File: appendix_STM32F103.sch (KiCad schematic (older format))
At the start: 69 parts, among them J201 Micro_SD_Card_Det, J202 Conn_02x05_Odd_Even, J203 Conn_02x20_Odd_Even, J204 Conn_ARM_JTAG_SWD_10, SW201 SW_Push, SW202 SW_Push, SW203 SW_Push, U201 STM32F103ZETx, U202 NTS0104PW-Q100J, U203 NTS0104PW-Q100J, X201 SG-210STF

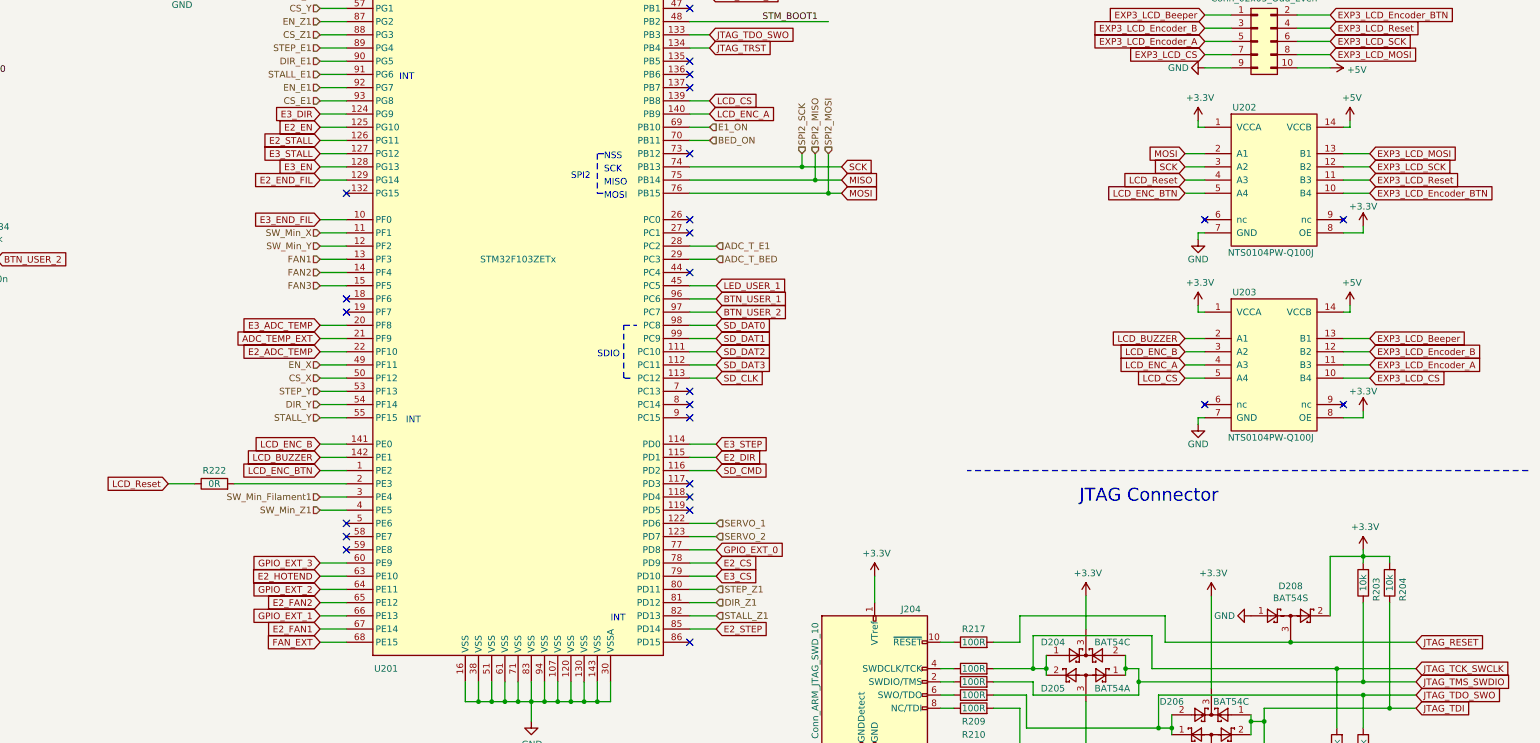
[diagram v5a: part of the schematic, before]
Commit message: changed Layout to use all Interrupt Pins
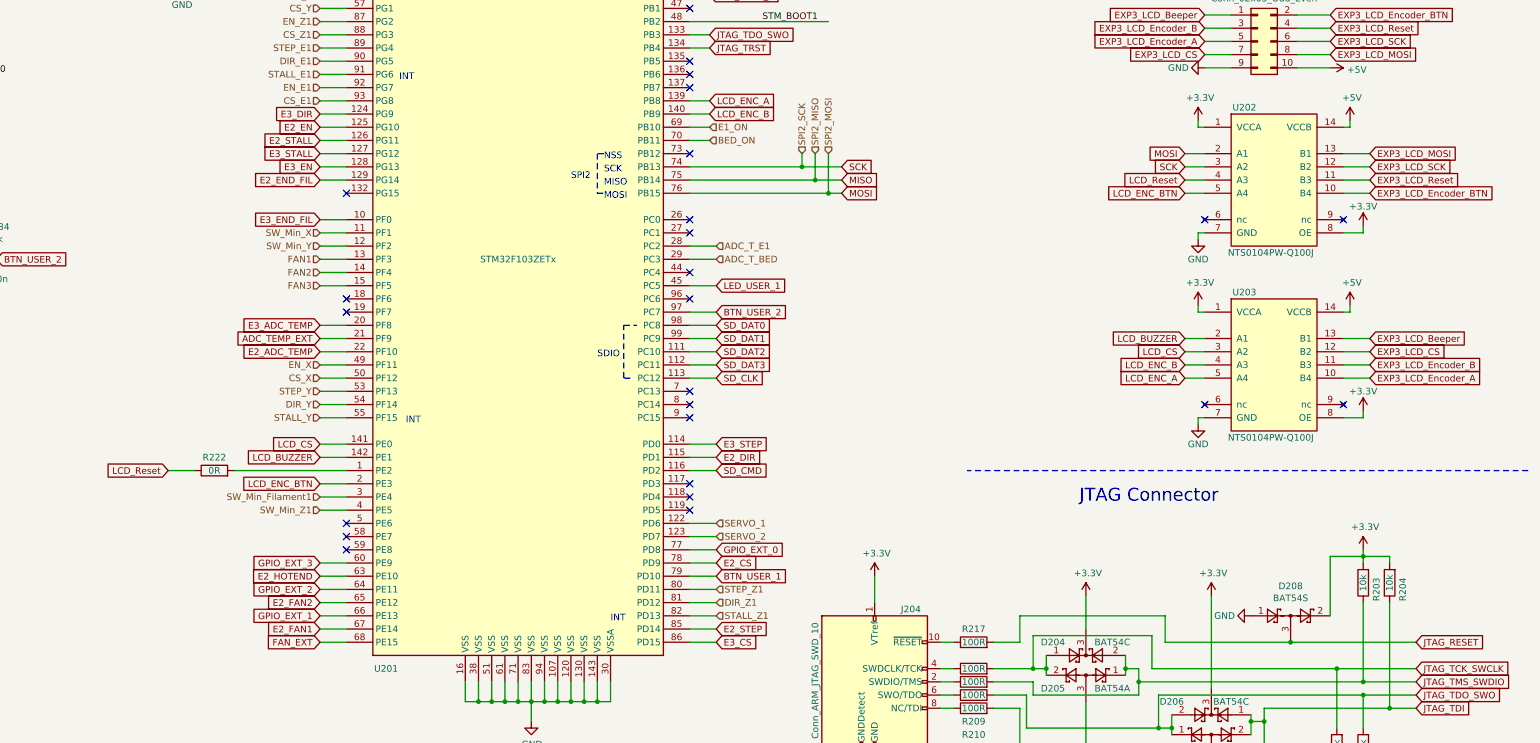
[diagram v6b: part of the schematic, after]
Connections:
- net BTN_USER_1: now also U201.79 (PD10); no longer U201.96 (PC6)
- net E3_CS: now also U201.86 (PD15); no longer U201.79 (PD10)
- net EXP3_LCD_CS: now also U203.12 (B2); no longer U203.10 (B4)
- net EXP3_LCD_Encoder_A: now also U203.10 (B4); no longer U203.11 (B3)
- net EXP3_LCD_Encoder_B: now also U203.11 (B3); no longer U203.12 (B2)
- net LCD_CS: now also U201.141 (PE0), U203.3 (A2); no longer U201.139 (PB8), U203.5 (A4)
- net LCD_ENC_A: now also U201.139 (PB8), U203.5 (A4); no longer U201.140 (PB9), U203.4 (A3)
- net LCD_ENC_B: now also U201.140 (PB9), U203.4 (A3); no longer U201.141 (PE0), U203.3 (A2)
- net LCD_ENC_BTN: now also U201.2 (PE3); no longer U201.1 (PE2)
- net at R222.2: now also U201.1 (PE2); no longer U201.2 (PE3)
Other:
- moved on the sheet: R222
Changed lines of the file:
@@
 Text GLabel 13600 3750 0    50   Input ~ 0
 EXP3_LCD_Beeper
+Text GLabel 14850 6300 2    50   Input ~ 0
+EXP3_LCD_CS
+Text GLabel 14850 6400 2    50   Input ~ 0
+EXP3_LCD_Encoder_B
 Text GLabel 14850 6500 2    50   Input ~ 0
-EXP3_LCD_CS
-Text GLabel 14850 6300 2    50   Input ~ 0
-EXP3_LCD_Encoder_B
-Text GLabel 14850 6400 2    50   Input ~ 0
 EXP3_LCD_Encoder_A
 Text GLabel 14850 6200 2    50   Input ~ 0
@@
 NoConn ~ 7100 7700
 NoConn ~ 7100 7800
-NoConn ~ 9700 8500
 NoConn ~ 9700 7400
 NoConn ~ 9700 7500
@@
 Wire Wire Line
 	7100 5500 6900 5500
-Text GLabel 6900 7200 0    50   Input ~ 0
+Text GLabel 6900 7300 0    50   Input ~ 0
 LCD_ENC_BTN
-Wire Wire Line
-	7100 7200 6900 7200
 Text GLabel 6900 7100 0    50   Input ~ 0
 LCD_BUZZER
+Text GLabel 9850 4500 2    50   Input ~ 0
+LCD_ENC_B
+Text GLabel 9850 4400 2    50   Input ~ 0
+LCD_ENC_A
 Text GLabel 6900 7000 0    50   Input ~ 0
-LCD_ENC_B
-Text GLabel 9850 4500 2    50   Input ~ 0
-LCD_ENC_A
-Text GLabel 9850 4400 2    50   Input ~ 0
 LCD_CS
 Wire Wire Line
@@
 Wire Notes Line
 	16050 3150 11800 3150
+Text GLabel 13450 6300 0    50   Input ~ 0
+LCD_CS
+Text GLabel 13450 6400 0    50   Input ~ 0
+LCD_ENC_B
 Text GLabel 13450 6500 0    50   Input ~ 0
-LCD_CS
-Text GLabel 13450 6300 0    50   Input ~ 0
-LCD_ENC_B
-Text GLabel 13450 6400 0    50   Input ~ 0
 LCD_ENC_A
 Text GLabel 13450 6200 0    50   Input ~ 0
@@
 Wire Wire Line
 	9900 6000 9700 6000
-Text GLabel 9900 5900 2    50   Input ~ 0
+Text GLabel 9900 8000 2    50   Input ~ 0
 BTN_USER_1
-Wire Wire Line
-	9900 5900 9700 5900
 $Comp
 L power:+3.3V #PWR0258
@@
 Text GLabel 9900 7900 2    50   Input ~ 0
 E2_CS
-Text GLabel 9900 8000 2    50   Input ~ 0
+Text GLabel 9900 8500 2    50   Input ~ 0
 E3_CS
 Wire Wire Line
@@
 Wire Wire Line
 	9700 7900 9900 7900
-Wire Wire Line
-	9900 8000 9700 8000
 Text GLabel 9900 8400 2    50   Input ~ 0
 E2_STEP
@@
 Wire Wire Line
 	7100 4600 6900 4600
-Text GLabel 5750 7300 0    50   Input ~ 0
+Text GLabel 5750 7200 0    50   Input ~ 0
 LCD_Reset
 $Comp
 L Device:R R222
 U 1 1 5CCE79DA
-P 6100 7300
-F 0 "R222" V 6200 7300 50  0000 C CNN
-F 1 "0R" V 6100 7300 50  0000 C CNN
-F 2 "Resistors_SMD:R_0603" V 6030 7300 50  0001 C CNN
-F 3 "~" H 6100 7300 50  0001 C CNN
-	1    6100 7300
+P 6100 7200
+F 0 "R222" V 6200 7200 50  0000 C CNN
+F 1 "0R" V 6100 7200 50  0000 C CNN
+F 2 "Resistors_SMD:R_0603" V 6030 7200 50  0001 C CNN
+F 3 "~" H 6100 7200 50  0001 C CNN
+	1    6100 7200
 	0    -1   -1   0
 $EndComp
 Wire Wire Line
-	5950 7300 5750 7300
-Wire Wire Line
-	7100 7300 6250 7300
+	5950 7200 5750 7200
+Wire Wire Line
+	7100 7200 6250 7200
 $Comp
 L power:+3.3VA #PWR0267
@@
 Wire Wire Line
 	7050 2400 7100 2400
+Wire Wire Line
+	9900 8500 9700 8500
+NoConn ~ 9700 5900
+Wire Wire Line
+	9900 8000 9700 8000
+Wire Wire Line
+	6900 7300 7100 7300
 $EndSCHEMATC

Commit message: fixed last minor issues
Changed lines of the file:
@@
 Wire Wire Line
 	6900 7300 7100 7300
+Text Notes 7500 5350 0    50   ~ 0
+INT
+Text Notes 7500 5450 0    50   ~ 0
+INT
+Text Notes 7500 5550 0    50   ~ 0
+INT
+Text Notes 7550 7350 0    50   ~ 0
+INT
+Text Notes 7550 7450 0    50   ~ 0
+INT
+Text Notes 7550 7550 0    50   ~ 0
+INT
+Text Notes 9150 2650 0    50   ~ 0
+INT
+Text Notes 9150 4450 0    50   ~ 0
+INT
+Text Notes 9150 4550 0    50   ~ 0
+INT
+Text Notes 9100 8050 0    50   ~ 0
+INT
+Text Notes 7550 4750 0    50   ~ 0
+INT
+Text Notes 7550 4850 0    50   ~ 0
+INT
+Text Notes 7550 5050 0    50   ~ 0
+INT
 $EndSCHEMATC

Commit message: Added comments to the schematic. Changed various component values (annotated only).
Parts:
- C201, C202, C203, C204, C205, C206, C207, C208, C209, C210, C211, C212, C213, C214, C215, C216, C220: symbol Device:C -> FHNW-Pro4E-FS19T8-3DPrinterBoard-STM32-rescue:C-Device
- C217, C218, C219: symbol Device:CP -> FHNW-Pro4E-FS19T8-3DPrinterBoard-STM32-rescue:CP-Device
- D201, D202, D203: symbol Device:LED -> FHNW-Pro4E-FS19T8-3DPrinterBoard-STM32-rescue:LED-Device
- D204, D206: symbol Diode:BAT54C -> FHNW-Pro4E-FS19T8-3DPrinterBoard-STM32-rescue:BAT54C-Diode
- D205, D207: symbol Diode:BAT54A -> FHNW-Pro4E-FS19T8-3DPrinterBoard-STM32-rescue:BAT54A-Diode
- D208: symbol Diode:BAT54S -> FHNW-Pro4E-FS19T8-3DPrinterBoard-STM32-rescue:BAT54S-Diode
- J201: symbol Connector:Micro_SD_Card_Det -> FHNW-Pro4E-FS19T8-3DPrinterBoard-STM32-rescue:Micro_SD_Card_Det-Connector
- J202: symbol Connector_Generic:Conn_02x05_Odd_Even -> FHNW-Pro4E-FS19T8-3DPrinterBoard-STM32-rescue:Conn_02x05_Odd_Even-Connector_Generic
- J203: symbol Connector_Generic:Conn_02x20_Odd_Even -> FHNW-Pro4E-FS19T8-3DPrinterBoard-STM32-rescue:Conn_02x20_Odd_Even-Connector_Generic
- J204: symbol Connector:Conn_ARM_JTAG_SWD_10 -> FHNW-Pro4E-FS19T8-3DPrinterBoard-STM32-rescue:Conn_ARM_JTAG_SWD_10-Connector
- R201, R202, R203, R204, R205, R206, R207, R208, R209, R210, R211, R212, R213, R214, R215, R216, R217, R218, R219, R220, R221, R222, R227, R229, R230, R231, R233, R234, R236, R237: symbol Device:R -> FHNW-Pro4E-FS19T8-3DPrinterBoard-STM32-rescue:R-Device
- SW201, SW202, SW203: symbol Switch:SW_Push -> FHNW-Pro4E-FS19T8-3DPrinterBoard-STM32-rescue:SW_Push-Switch
- U201: symbol MCU_ST_STM32F1:STM32F103ZETx -> FHNW-Pro4E-FS19T8-3DPrinterBoard-STM32-rescue:STM32F103ZETx-MCU_ST_STM32F1
- X201: symbol Oscillator:SG-210STF -> FHNW-Pro4E-FS19T8-3DPrinterBoard-STM32-rescue:SG-210STF-Oscillator
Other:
- note added: "*) will be populated once ensured the ESP32\n will not pull those pins high/low unexpectedly"
- note added: "6 bypass capacitors missing!"
- note added: "Analog"
- note added: "Analog reference is missing."
- note added: "Could have used another bypass capacitor."
- note added: "DNP"
- note added: "DNP*"
- note added: "EXT1 (new)"
- note added: "EXT1 and EXT2 exchanged (fixed in the firmware)"
- note added: "EXT2 (new)"
- note added: "GREEN"
- note added: "Level shifter"
- note added: "Probably not the actual\nMOSI and SCK pins.\nTesting needed!"
- note added: "SD card"
- note added: "SD inserted => 0\nSD not inserted => 1"
- note added: "Wrongly labeled as EXT3 on the PCB."
- note added: "YELLOW"
- note added: "either R220 or R222 have to be populated,\n=> R220 will probably work fine"
